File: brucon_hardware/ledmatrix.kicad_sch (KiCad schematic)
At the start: 25 parts, among them U301 74HCT245, U302 TC7262C, U303 TC7262C, U304 TC7262C, U305 TC5020D, U306 TC5020D, U307 TC5020D, U308 TC5020D, U309 TC5020D, U310 TC5020D

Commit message: Updated part numbers
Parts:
- R301, R302, R303, R304, R305, R306: LCSC (none) -> C4177
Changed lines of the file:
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@@
 			)
 		)
-		(property "LCSC" ""
+		(property "LCSC" "C4177"
 			(at 994.41 270.51 0)
 			(effects
@@
 			)
 		)
-		(property "LCSC" ""
+		(property "LCSC" "C4177"
 			(at 991.87 140.97 0)
 			(effects
@@
 			)
 		)
-		(property "LCSC" ""
+		(property "LCSC" "C4177"
 			(at 990.6 100.33 0)
 			(effects
@@
 			)
 		)
-		(property "LCSC" ""
+		(property "LCSC" "C4177"
 			(at 993.14 229.87 0)
 			(effects
@@
 			)
 		)
-		(property "LCSC" ""
+		(property "LCSC" "C4177"
 			(at 989.33 59.69 0)
 			(effects
@@
 			)
 		)
-		(property "LCSC" ""
+		(property "LCSC" "C4177"
 			(at 991.87 189.23 0)
 			(effects

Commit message: Small changes
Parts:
- R301, R302, R303, R304, R305, R306: LCSC C4177 -> C25871
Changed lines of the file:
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@@
 			)
 		)
-		(property "LCSC" "C4177"
+		(property "LCSC" " C25871"
 			(at 994.41 270.51 0)
 			(effects
@@
 			)
 		)
-		(property "LCSC" "C4177"
+		(property "LCSC" " C25871"
 			(at 991.87 140.97 0)
 			(effects
@@
 			)
 		)
-		(property "LCSC" "C4177"
+		(property "LCSC" " C25871"
 			(at 990.6 100.33 0)
 			(effects
@@
 			)
 		)
-		(property "LCSC" "C4177"
+		(property "LCSC" " C25871"
 			(at 993.14 229.87 0)
 			(effects
@@
 			)
 		)
-		(property "LCSC" "C4177"
+		(property "LCSC" " C25871"
 			(at 989.33 59.69 0)
 			(effects
@@
 			)
 		)
-		(property "LCSC" "C4177"
+		(property "LCSC" " C25871"
 			(at 991.87 189.23 0)
 			(effects

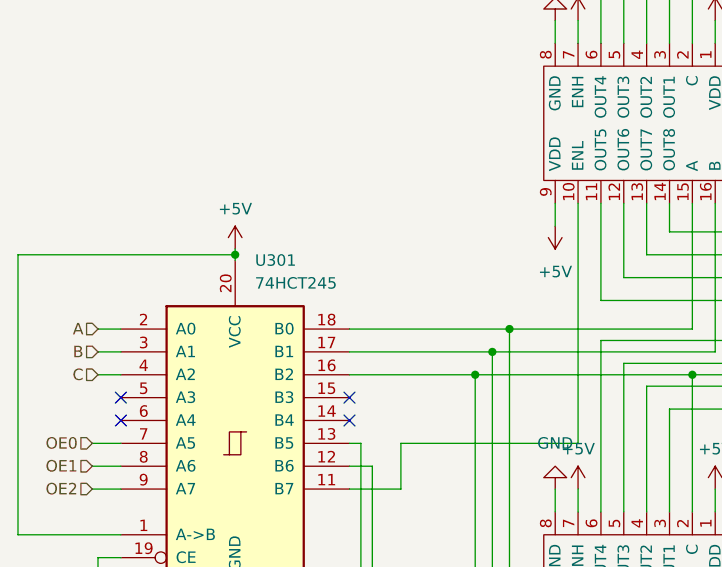
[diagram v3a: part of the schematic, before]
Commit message: Swapped IP5305 for IP5305T (needs current limiting resistors on LEDs), swapped buffer for Nexperia alternative for availability and price. Ordered 2nd prototype.
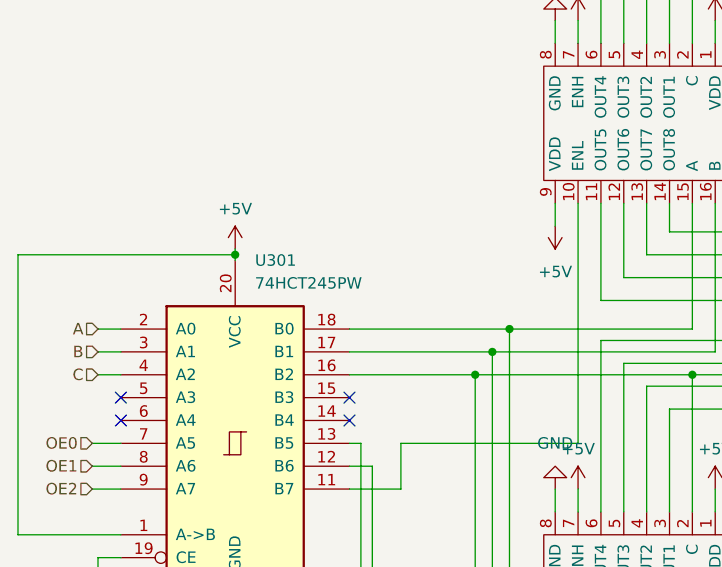
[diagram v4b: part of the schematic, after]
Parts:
- U301: value 74HCT245 -> 74HCT245PW; LCSC C7494911 -> C5980
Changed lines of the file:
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@@
 			)
 		)
-		(property "Value" "74HCT245"
+		(property "Value" "74HCT245PW"
 			(at 315.8841 433.07 0)
 			(effects
@@
 			)
 		)
-		(property "Datasheet" "http://www.ti.com/lit/gpn/sn74HC245"
+		(property "Datasheet" "https://www.lcsc.com/datasheet/lcsc_datasheet_2304140030_Nexperia-74HCT245PW-118_C5980.pdf"
 			(at 313.69 450.85 0)
 			(effects
@@
 			)
 		)
-		(property "LCSC" "C7494911"
+		(property "LCSC" "C5980"
 			(at 313.69 450.85 0)
 			(effects
